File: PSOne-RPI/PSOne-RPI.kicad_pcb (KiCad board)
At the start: 2 copper layers, 166 x 124 mm, 53 parts, among them J1 M.2 (PCIe / NVMe), J10 Controller-Port, J11 Controller-Port, J12 Micro_SD_Card, J13 USB_3_4, J14 FAN1, J15 CN701, J16 CN702, J2 RaspberryPi4-ComputeModule, J3 Combined-Connector-Back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

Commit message: Finished CD drive interface circuit
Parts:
- removed J16: CN702, PSOne-RPI:FFC-1x16-Vertical
- added C10: 82nF, Capacitor_SMD:C_1206_3216Metric, F.Cu at (149.0, 127.6)
- added C11: 82nF, Capacitor_SMD:C_1206_3216Metric, F.Cu at (141.2, 112.8)
- added C9: 33uF, Capacitor_SMD:C_1206_3216Metric, F.Cu at (145.4, 126.4)
- added J9: FAN1, Connector_Hirose:Hirose_DF13-02P-1.25DSA_1x02_P1.25mm_Vertical, F.Cu at (161.6, 115.4)
- added L2: 10uH, Inductor_SMD:L_1812_4532Metric, F.Cu at (142.9, 119.2)
- added Q1: 2SB1132, Package_TO_SOT_SMD:SOT-23, F.Cu at (146.6, 123.2)
- added R10: 33k, Resistor_SMD:R_1206_3216Metric, F.Cu at (138.2, 122.0)
- added R11: 33k, Resistor_SMD:R_1206_3216Metric, F.Cu at (135.8, 122.0)
- added R12: 33k, Resistor_SMD:R_1206_3216Metric, F.Cu at (134.6, 117.2)
- added R13: 33k, Resistor_SMD:R_1206_3216Metric, F.Cu at (137.0, 117.2)
- added R14: 91, Resistor_SMD:R_1206_3216Metric, F.Cu at (133.4, 122.0)
- added R5: 22, Resistor_SMD:R_1206_3216Metric, F.Cu at (141.6, 127.6)
- added R9: 22, Resistor_SMD:R_1206_3216Metric, F.Cu at (145.4, 129.0)
- J14: value FAN1 -> CN701; footprint Connector_Hirose:Hirose_DF13-02P-1.25DSA_1x02_P1.25mm_Vertical -> Connector_Hirose:Hirose_DF13-04P-1.25DSA_1x04_P1.25mm_Vertical
- J15: value CN701 -> CN702; footprint Connector_Hirose:Hirose_DF13-04P-1.25DSA_1x04_P1.25mm_Vertical -> PSOne-RPI:FFC-1x16-Vertical
- moved D6 37.8 mm to (154.4, 129.0), turned to 90 degrees
- moved D7 34.7 mm to (122.8, 122.2)
- moved D4 34.5 mm to (158.2, 129.0), turned to 90 degrees
- moved D8 33.5 mm to (119.2, 122.2)
- moved F3 29.8 mm to (117.6, 116.4), turned to 180 degrees
- moved J15 29.3 mm to (130.0, 128.4), turned to 180 degrees
- moved U6 26.0 mm to (153.2, 116.2), turned to 0 degrees
- moved U5 23.9 mm to (127.0, 115.2), turned to 270 degrees
- moved J14 13.4 mm to (159.2, 124.6), turned to 0 degrees
- moved D5 6.37 mm to (126.4, 122.2)
- moved D3 4.67 mm to (130.0, 122.2)
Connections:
- D2 pad 4: /STM32F103/+3.3V -> /+3.3V_STB
- D3 pad 3: Net-(D3-Pad3) -> /CD-Interface/CD_FSC_DRV_A
- D4 pad 2: /+3.3V_STB -> /+5V
- D4 pad 3: Net-(D4-Pad3) -> /CD-Interface/CD_OPT_DRV_A
- D5 pad 3: Net-(D5-Pad3) -> /CD-Interface/CD_TRC_DRV_A
- D6 pad 2: /+3.3V_STB -> /+5V
- D6 pad 3: Net-(D6-Pad3) -> /CD-Interface/CD_OPT_DRV_B
- D7 pad 2: /+5V -> /+3.3V_STB
- D7 pad 3: Net-(D7-Pad3) -> /CD-Interface/CD_TRC_DRV_B
- D8 pad 2: /+5V -> /+3.3V_STB
- D8 pad 3: Net-(D8-Pad3) -> /CD-Interface/CD_FSC_DRV_B
- F3 pad 2: /STM32F103/+3.3V -> /CD-Interface/+3.3V_CP
- J10 pad 14: /STM32F103/+3.3V -> /CD-Interface/+3.3V_CP
- J10 pad 5: /STM32F103/+3.3V -> /CD-Interface/+3.3V_CP
- J11 pad 14: /STM32F103/+3.3V -> /CD-Interface/+3.3V_CP
- J11 pad 5: /STM32F103/+3.3V -> /CD-Interface/+3.3V_CP
- J14 pad 1: Net-(J14-Pad1) -> /CD-Interface/CD_OPT_DRV_B
- J14 pad 2: GND -> /CD-Interface/CD_OPT_DRV_A
- J15 pad 1: Net-(D8-Pad3) -> Net-(C11-Pad2)
- J15 pad 2: Net-(D7-Pad3) -> /CD-Interface/+3.3V_CP
- J15 pad 3: Net-(J15-Pad3) -> /+3.3V_STB
- J15 pad 4: GND -> Net-(J15-Pad4)
- J4 pad 17: /Raspberry-Pi-Highspeed/CAM_GPIO -> /Raspberry-Pi-GPIO/CAM_GPIO
- J5 pad 17: /Raspberry-Pi-Highspeed/CAM_GPIO -> /Raspberry-Pi-GPIO/CAM_GPIO
- U5 pad 1: /STM32F103/FAN -> /CD-Interface/CD_FSC_A
- U5 pad 10: Net-(U5-Pad10) -> Net-(F3-Pad1)
- U5 pad 11: Net-(D8-Pad3) -> Net-(F3-Pad1)
- U5 pad 12: Net-(D7-Pad3) -> Net-(U5-Pad12)
- U5 pad 13: Net-(J15-Pad3) -> /CD-Interface/CD_FSC_DRV_B
- U5 pad 14: Net-(J15-Pad3) -> /CD-Interface/CD_TRC_DRV_B
- U5 pad 15: Net-(J14-Pad1) -> /CD-Interface/CD_TRC_DRV_A
- U5 pad 16: Net-(J14-Pad1) -> /CD-Interface/CD_FSC_DRV_A
- U5 pad 2: /STM32F103/FAN -> /CD-Interface/CD_TRC_A
- U5 pad 3: /STM32F103/CD_DISK -> /CD-Interface/CD_TRC_B
- U5 pad 4: /STM32F103/CD_DISK -> /CD-Interface/CD_FSC_B
- U5 pad 5: /STM32F103/CD_OPT_A -> Net-(U5-Pad5)
- U5 pad 6: /STM32F103/CD_OPT_B -> /CD-Interface/+3.3V_EN
- U5 pad 7: Net-(U5-Pad7) -> /CD-Interface/+3.3V_EN
- U5 pad 9: /+5V -> /+3.3V_STB
- U6 pad 1: /STM32F103/CD_FSC_A -> /CD-Interface/PWM_FAN
- U6 pad 10: Net-(F3-Pad1) -> Net-(U6-Pad10)
- U6 pad 11: Net-(F3-Pad1) -> /CD-Interface/CD_OPT_DRV_B
- U6 pad 12: Net-(U6-Pad12) -> /CD-Interface/CD_OPT_DRV_A
- U6 pad 13: Net-(D6-Pad3) -> /CD-Interface/CD_DISK_DRV
- U6 pad 14: Net-(D5-Pad3) -> /CD-Interface/CD_DISK_DRV
- U6 pad 15: Net-(D4-Pad3) -> /CD-Interface/PWM_FAN_DRV
- U6 pad 16: Net-(D3-Pad3) -> /CD-Interface/PWM_FAN_DRV
- U6 pad 2: /STM32F103/CD_TRC_A -> /CD-Interface/PWM_FAN
- U6 pad 3: /STM32F103/CD_TRC_B -> /CD-Interface/CD_DISK
- U6 pad 4: /STM32F103/CD_FSC_B -> /CD-Interface/CD_DISK
- U6 pad 5: Net-(U6-Pad5) -> /CD-Interface/CD_OPT_A
- U6 pad 6: /STM32F103/+3.3V_EN -> /CD-Interface/CD_OPT_B
- U6 pad 7: /STM32F103/+3.3V_EN -> Net-(U6-Pad7)
- U6 pad 9: /+3.3V_STB -> /+5V
- U7 pad 10: Net-(U7-Pad10) -> /CD-Interface/CD_RD_C
- U7 pad 11: Net-(U7-Pad11) -> /CD-Interface/CD_RD_D
- U7 pad 15: /STM32F103/CD_DISK -> /CD-Interface/CD_DISK
- U7 pad 16: /STM32F103/CD_OPT_A -> /CD-Interface/CD_OPT_A
- U7 pad 17: /STM32F103/CD_OPT_B -> /CD-Interface/CD_OPT_B
- U7 pad 20: /STM32F103/CD_RD_A -> /CD-Interface/CD_STOP
- U7 pad 21: /STM32F103/CD_RD_B -> /CD-Interface/CD_LD
- U7 pad 22: /STM32F103/CD_RD_C -> /CD-Interface/CD_MD
- U7 pad 23: /STM32F103/CD_RD_D -> Net-(U7-Pad23)
- U7 pad 27: /STM32F103/FAN -> /CD-Interface/PWM_FAN
- U7 pad 37: /STM32F103/CD_FSC_A -> /CD-Interface/CD_FSC_A
- U7 pad 38: /STM32F103/CD_TRC_A -> /CD-Interface/CD_TRC_A
- U7 pad 39: /STM32F103/CD_TRC_B -> /CD-Interface/CD_TRC_B
- U7 pad 40: /STM32F103/CD_FSC_B -> /CD-Interface/CD_FSC_B
- U7 pad 46: /STM32F103/+3.3V_EN -> /CD-Interface/+3.3V_CP_EN
- U7 pad 8: Net-(U7-Pad8) -> /CD-Interface/CD_RD_A
- U7 pad 9: Net-(U7-Pad9) -> /CD-Interface/CD_RD_B
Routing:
- net /STM32F103/+3.3V: track 71.7 -> 0.00 mm
- net /CD-Interface/+3.3V_CP: track 0.00 -> 71.7 mm

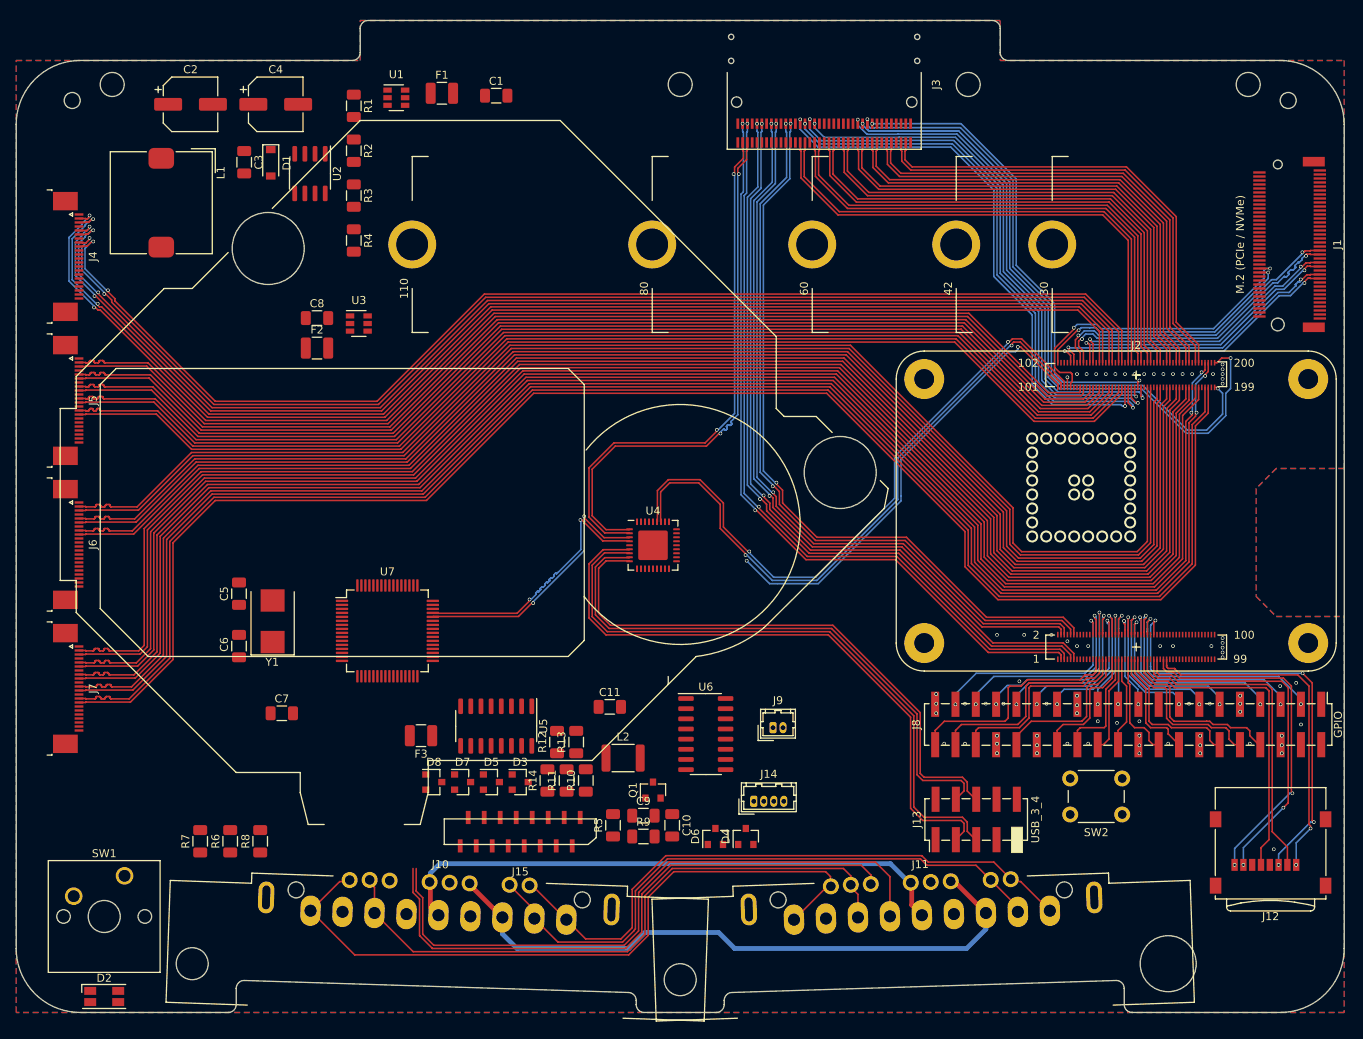
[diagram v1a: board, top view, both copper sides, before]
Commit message: Updated internal power supply
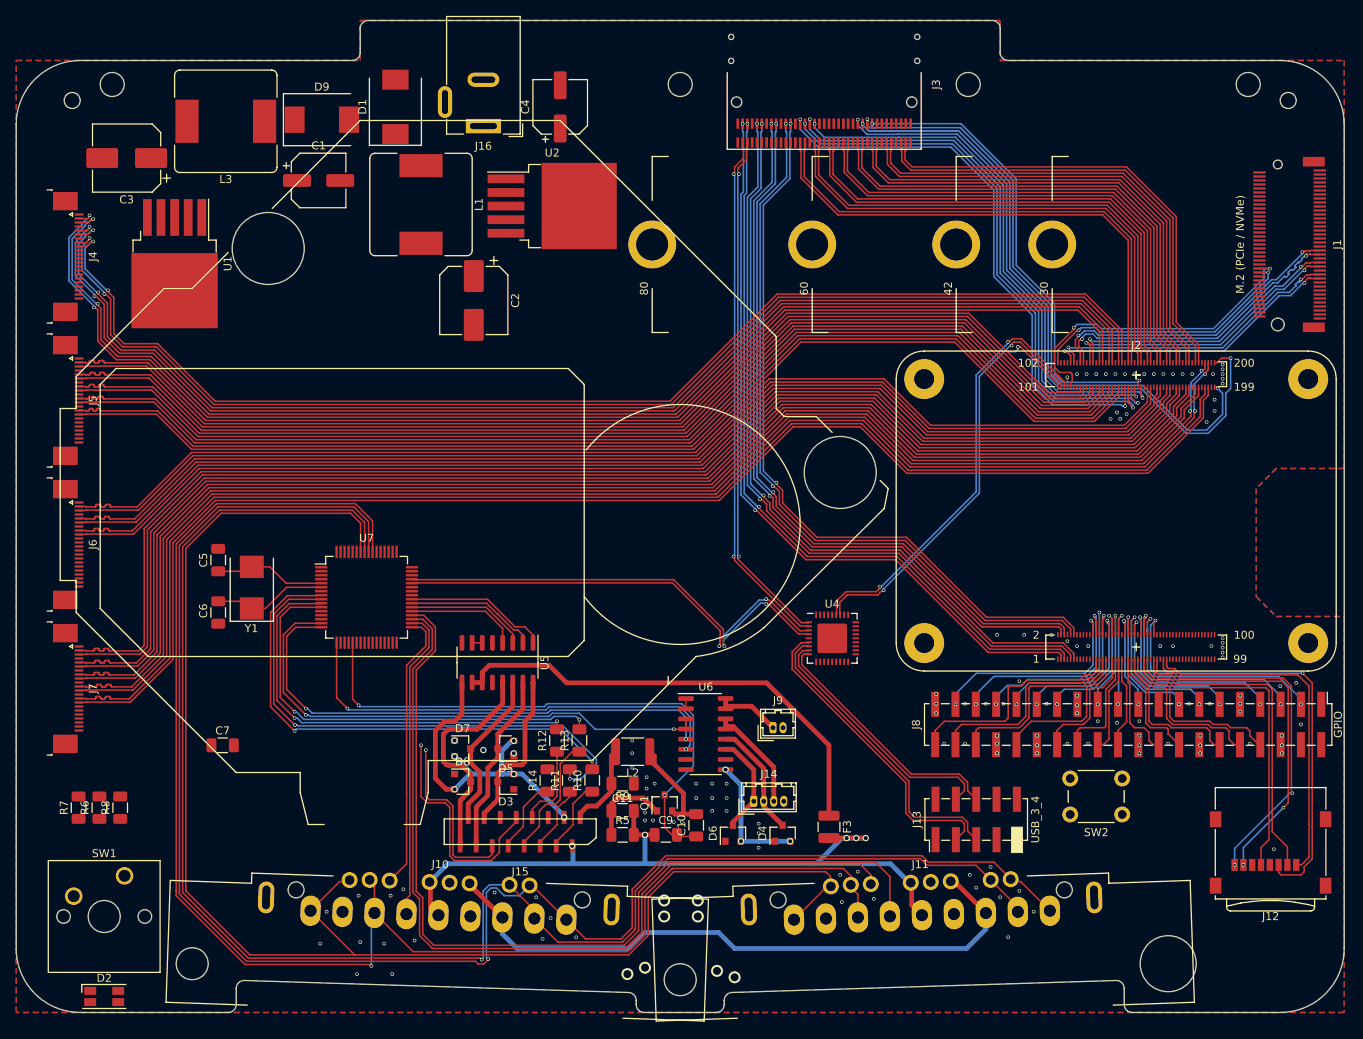
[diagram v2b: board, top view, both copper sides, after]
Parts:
- removed C8: 1uF, Capacitor_SMD:C_1206_3216Metric
- removed F1, F2: 750mA, Fuse:Fuse_1210_3225Metric
- removed R1: 0.22, Resistor_SMD:R_1206_3216Metric
- removed R2: 180, Resistor_SMD:R_1206_3216Metric
- removed R3, R4: 10k, Resistor_SMD:R_1206_3216Metric
- removed U3: TPS22929D, Package_TO_SOT_SMD:SOT-23-6
- added D9: B330, Diode_SMD:D_SMC, F.Cu at (105.2, 39.4)
- added J16: +7.5V / 2.2A, Connector_BarrelJack:BarrelJack_Wuerth_6941xx301002, F.Cu at (125.4, 40.2)
- added L3: 100uH, Inductor_SMD:L_Bourns_SRR1260, F.Cu at (93.2, 39.6)
- C1: value 1uF -> 100uF; footprint Capacitor_SMD:C_1206_3216Metric -> Capacitor_SMD:CP_Elec_6.3x5.8
- C2: value 100uF -> 1000uF; footprint Capacitor_SMD:CP_Elec_6.3x5.9 -> Capacitor_SMD:CP_Elec_8x6.5
- C3: value 1500pF -> 1000uF; footprint Capacitor_SMD:C_1206_3216Metric -> Capacitor_SMD:CP_Elec_8x6.5
- C4: value 330uF -> 100uF; footprint Capacitor_SMD:CP_Elec_6.3x5.9 -> Capacitor_SMD:CP_Elec_6.3x5.8
- D1: value PMEG6010CEH -> B330; footprint Diode_SMD:D_SOD-123 -> Diode_SMD:D_SMC
- L1: value 170uH -> 100uH; footprint Inductor_SMD:L_TDK_SLF12575 -> Inductor_SMD:L_Bourns_SRR1260
- U1: value TPS22929D -> LM2576S-3.3; footprint Package_TO_SOT_SMD:SOT-23-6 -> Package_TO_SOT_SMD:TO-263-5_TabPin3
- U2: value MC34063AD -> LM2576S-5; footprint Package_SO:SOIC-8_3.9x4.9mm_P1.27mm -> Package_TO_SOT_SMD:TO-263-5_TabPin3
- moved F3 52.3 mm to (168.6, 127.8), turned to 270 degrees
- moved C2 43.1 mm to (124.2, 62.0), turned to 270 degrees
- moved C4 35.6 mm to (135.0, 37.8), turned to 90 degrees
- moved U1 34.6 mm to (86.8, 57.4), turned to 270 degrees
- moved L1 32.5 mm to (117.6, 50.0)
- moved U2 30.6 mm to (134.0, 50.2), turned to 0 degrees
- moved U4 25.2 mm to (169.0, 104.2)
- moved C1 24.6 mm to (104.8, 47.0)
- moved R8 18.0 mm to (80.0, 125.4)
- moved D1 17.1 mm to (114.4, 37.8), turned to 90 degrees
- moved R6 16.9 mm to (77.4, 125.4)
- moved R7 15.8 mm to (74.8, 125.4)
- moved C3 14.7 mm to (80.8, 44.2), turned to 180 degrees
- moved C11 9.73 mm to (142.8, 122.4), turned to 180 degrees
- moved C7 8.41 mm to (92.8, 117.6)
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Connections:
- C1 pad 1: GND -> /+5V_STB
- C1 pad 2: /+5V_STB -> GND
- C2 pad 1: /Power Supply/+5V_B_SW -> /+5V_STB
- C3 pad 1: GND -> /+3.3V_STB
- C3 pad 2: Net-(C3-Pad2) -> GND
- C4 pad 1: /Power Supply/+9V -> /+7.5V
- D1 pad 1: /Power Supply/+9V -> Net-(D1-Pad1)
- D1 pad 2: Net-(D1-Pad2) -> GND
- L1 pad 1: Net-(L1-Pad1) -> Net-(D1-Pad1)
- L1 pad 2: Net-(D1-Pad2) -> /+5V_STB
- U1 pad 1: Net-(F1-Pad1) -> /+5V_STB
- U1 pad 2: GND -> Net-(D9-Pad1)
- U1 pad 3: /+5V_EN -> GND
- U1 pad 4: /+5V_STB -> /+3.3V_STB
- U2 pad 1: Net-(D1-Pad2) -> /+7.5V
- U2 pad 2: GND -> Net-(D1-Pad1)
- U2 pad 3: Net-(C3-Pad2) -> GND
- U2 pad 4: GND -> /+5V_STB
- U2 pad 5: Net-(R3-Pad1) -> GND
- U7 pad 28: /STM32F103/ACK -> Net-(U7-Pad28)
- U7 pad 33: /STM32F103/CP1_SEL -> /STM32F103/MEM1_SEL
- U7 pad 34: /STM32F103/MEM1_SEL -> /STM32F103/CP1_SEL
- U7 pad 35: /STM32F103/CP2_SEL -> /STM32F103/MEM2_SEL
- U7 pad 36: /STM32F103/MEM2_SEL -> /STM32F103/CP2_SEL
- U7 pad 37: /CD-Interface/CD_FSC_A -> /CD-Interface/CD_FSC_B
- U7 pad 38: /CD-Interface/CD_TRC_A -> /CD-Interface/CD_TRC_B
- U7 pad 39: /CD-Interface/CD_TRC_B -> /CD-Interface/CD_TRC_A
- U7 pad 40: /CD-Interface/CD_FSC_B -> /CD-Interface/CD_FSC_A
- U7 pad 58: Net-(U7-Pad58) -> /STM32F103/ACK
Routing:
- net /STM32F103/DATA: track 77.3 -> 208.6 mm, vias 0 -> 1
- net /STM32F103/CMD: track 77.0 -> 202.3 mm, vias 0 -> 1
- net /STM32F103/CLK: track 78.7 -> 188.9 mm, vias 0 -> 1
- net /STM32F103/ACK: track 88.6 -> 183.6 mm
- net /CD-Interface/CD_LD: track 0.00 -> 70.7 mm, vias 0 -> 2
- net /CD-Interface/CD_RD_B: track 0.00 -> 67.0 mm, vias 0 -> 2
- net /CD-Interface/CD_DISK: track 0.00 -> 66.4 mm, vias 0 -> 2
- net /CD-Interface/CD_OPT_A: track 0.00 -> 65.8 mm, vias 0 -> 2
- net /CD-Interface/CD_RD_A: track 0.00 -> 63.2 mm, vias 0 -> 2
- net Net-(F3-Pad1): track 0.00 -> 59.2 mm
- net /CD-Interface/CD_OPT_B: track 0.00 -> 56.7 mm, vias 0 -> 2
- net /CD-Interface/CD_RD_D: track 0.00 -> 55.7 mm, vias 0 -> 2
- net /CD-Interface/CD_RD_C: track 0.00 -> 54.0 mm, vias 0 -> 2
- net Net-(J2-Pad101): track 57.9 -> 8.93 mm, vias 2 -> 1
- net /+3.3V_STB: track 0.00 -> 42.0 mm, vias 0 -> 5
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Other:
- net class Power: clearance 0.5 -> 0.4; via_drill 0.6 -> 0.5

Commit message: Added possibility to use the STM32 as RTC
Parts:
- added BT1: Battery_Cell, Battery:BatteryHolder_Keystone_1058_1x2032, F.Cu at (88.0, 118.6)
- moved R7 64.3 mm to (132.6, 97.2), turned to 270 degrees
- moved R8 62.0 mm to (135.2, 97.2), turned to 270 degrees
- moved R6 59.7 mm to (130.0, 97.2), turned to 270 degrees
- moved C7 27.4 mm to (99.4, 91.0)
- moved J4 5.34 mm to (72.3, 51.3)
- moved J5 5.34 mm to (72.3, 69.3)
- moved J6 5.34 mm to (72.3, 87.3)
- moved J7 5.34 mm to (72.3, 105.3)
- turned D2 to 180 degrees
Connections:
- J16 pad 1: Net-(J16-Pad1) -> /+7.5V
- J16 pad 2: Net-(J16-Pad2) -> GND
- J16 pad 3: Net-(J16-Pad3) -> GND
- J2 pad 80: Net-(J2-Pad80) -> /STM32F103/SCL
- J2 pad 82: Net-(J2-Pad82) -> /STM32F103/SDA
- U7 pad 1: /+3.3V_STB -> /STM32F103/V_BAT
- U7 pad 61: Net-(U7-Pad61) -> /STM32F103/SCL
- U7 pad 62: Net-(U7-Pad62) -> /STM32F103/SDA
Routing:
- net Net-(D2-Pad3): track 0.00 -> 122.6 mm
- net Net-(D2-Pad2): track 0.00 -> 116.6 mm
- net Net-(D2-Pad1): track 0.00 -> 114.7 mm
- net /STM32F103/LED_B: track 0.00 -> 20.3 mm
- net /STM32F103/LED_G: track 0.00 -> 17.6 mm
- net /STM32F103/LED_R: track 0.00 -> 14.2 mm
- net /Raspberry-Pi-Highspeed/DSI1_D0_N: track 165.9 -> 163.5 mm
- net /Raspberry-Pi-Highspeed/DSI1_D1_N: track 167.8 -> 165.7 mm
- net /Raspberry-Pi-Highspeed/CAM1_D3_N: track 144.1 -> 142.1 mm
- net /Raspberry-Pi-Highspeed/DSI1_D0_P: track 165.9 -> 164.1 mm
- net /Raspberry-Pi-Highspeed/DSI1_C_N: track 169.6 -> 167.8 mm
- net /Raspberry-Pi-Highspeed/DSI0_D0_N: track 146.3 -> 144.7 mm
- net /Raspberry-Pi-Highspeed/DSI0_C_N: track 150.0 -> 148.3 mm
- net /Raspberry-Pi-Highspeed/DSI0_D1_N: track 148.1 -> 146.5 mm
- net /Raspberry-Pi-Highspeed/CAM0_D0_N: track 159.8 -> 161.3 mm
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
